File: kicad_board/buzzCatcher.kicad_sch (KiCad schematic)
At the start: 38 parts, among them IC1 TS02-66-60-BK-100-SCR-D, J1 95501-2661, J10 M5 Screw, J11 M5 Screw, J12 M5 Screw, J13 25 ft RJ12, J14 25 ft RJ12, J15 25 ft RJ12, J16 25 ft RJ12, J2 95501-2661, J3 95501-2661, J4 95501-2661, J5 95501-2661, J6 95501-2661, J7 95501-2661, J8 95501-2661, J9 M5 Screw, Q1 BS170, Q2 BS170, SW1 SW_Push, SW2 SW_Push, SW3 SW_Push, SW4 SW_Push

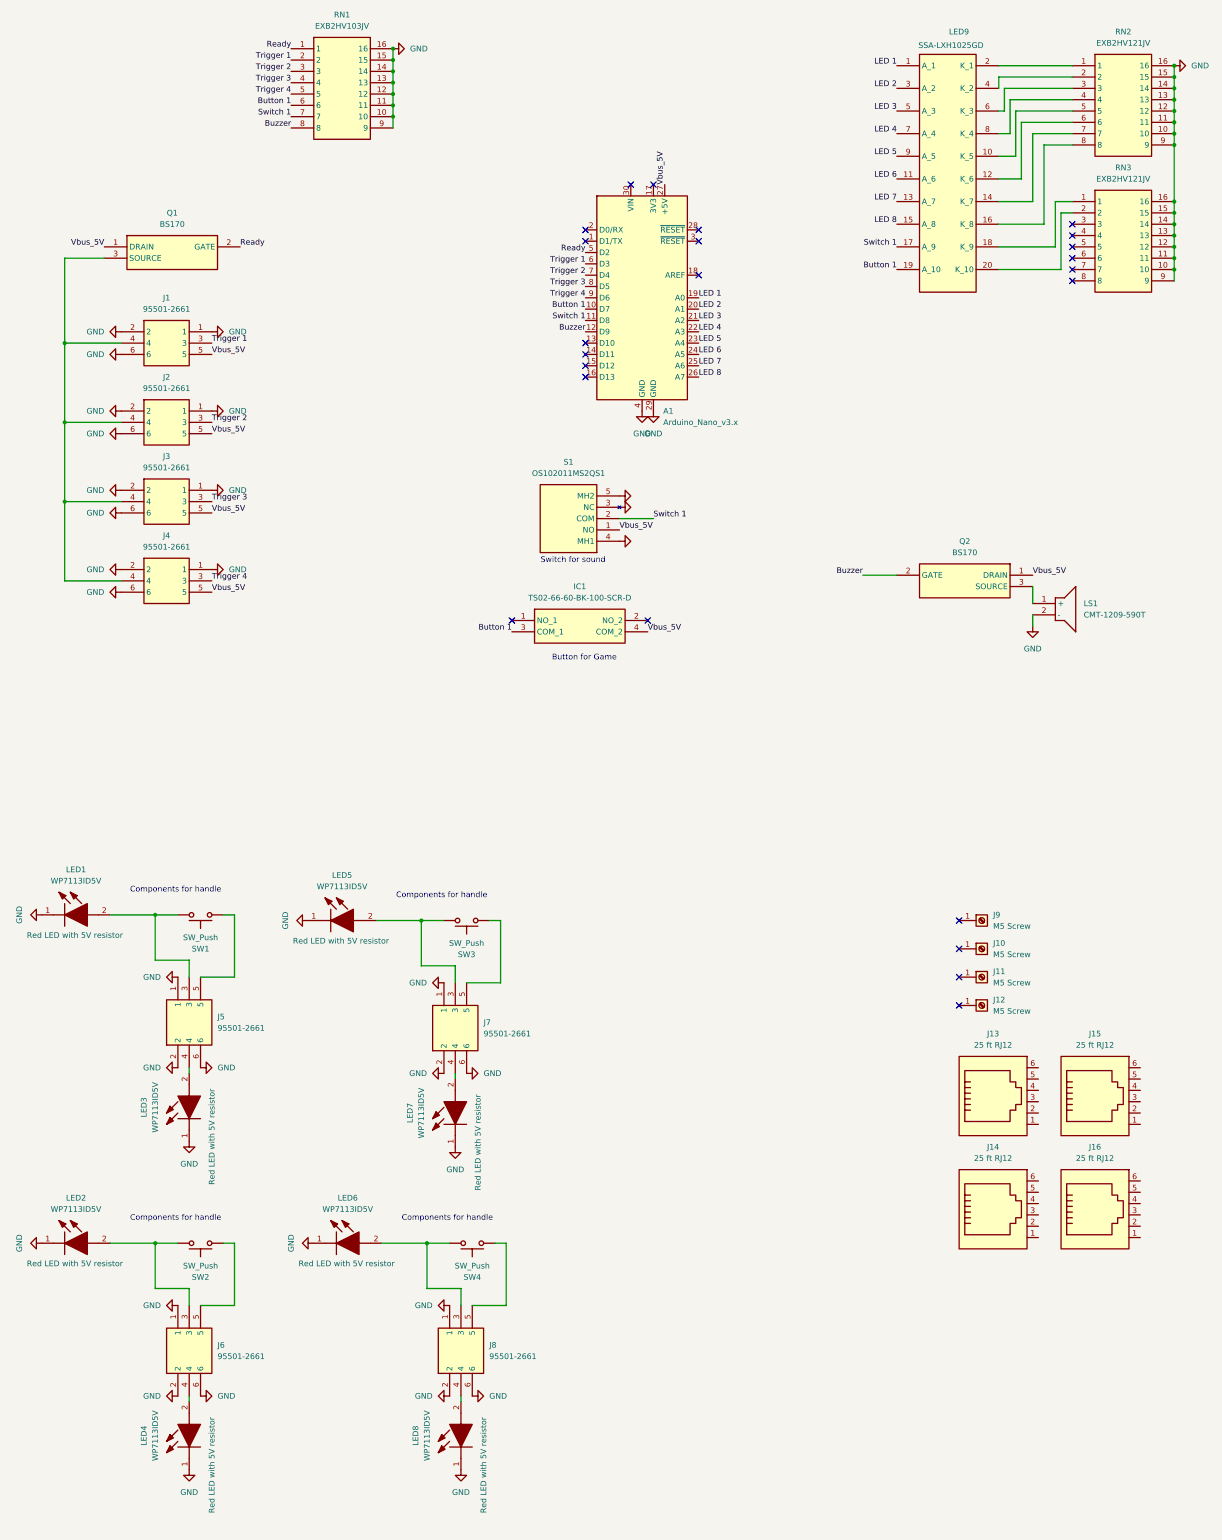
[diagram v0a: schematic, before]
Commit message: Added break out headers
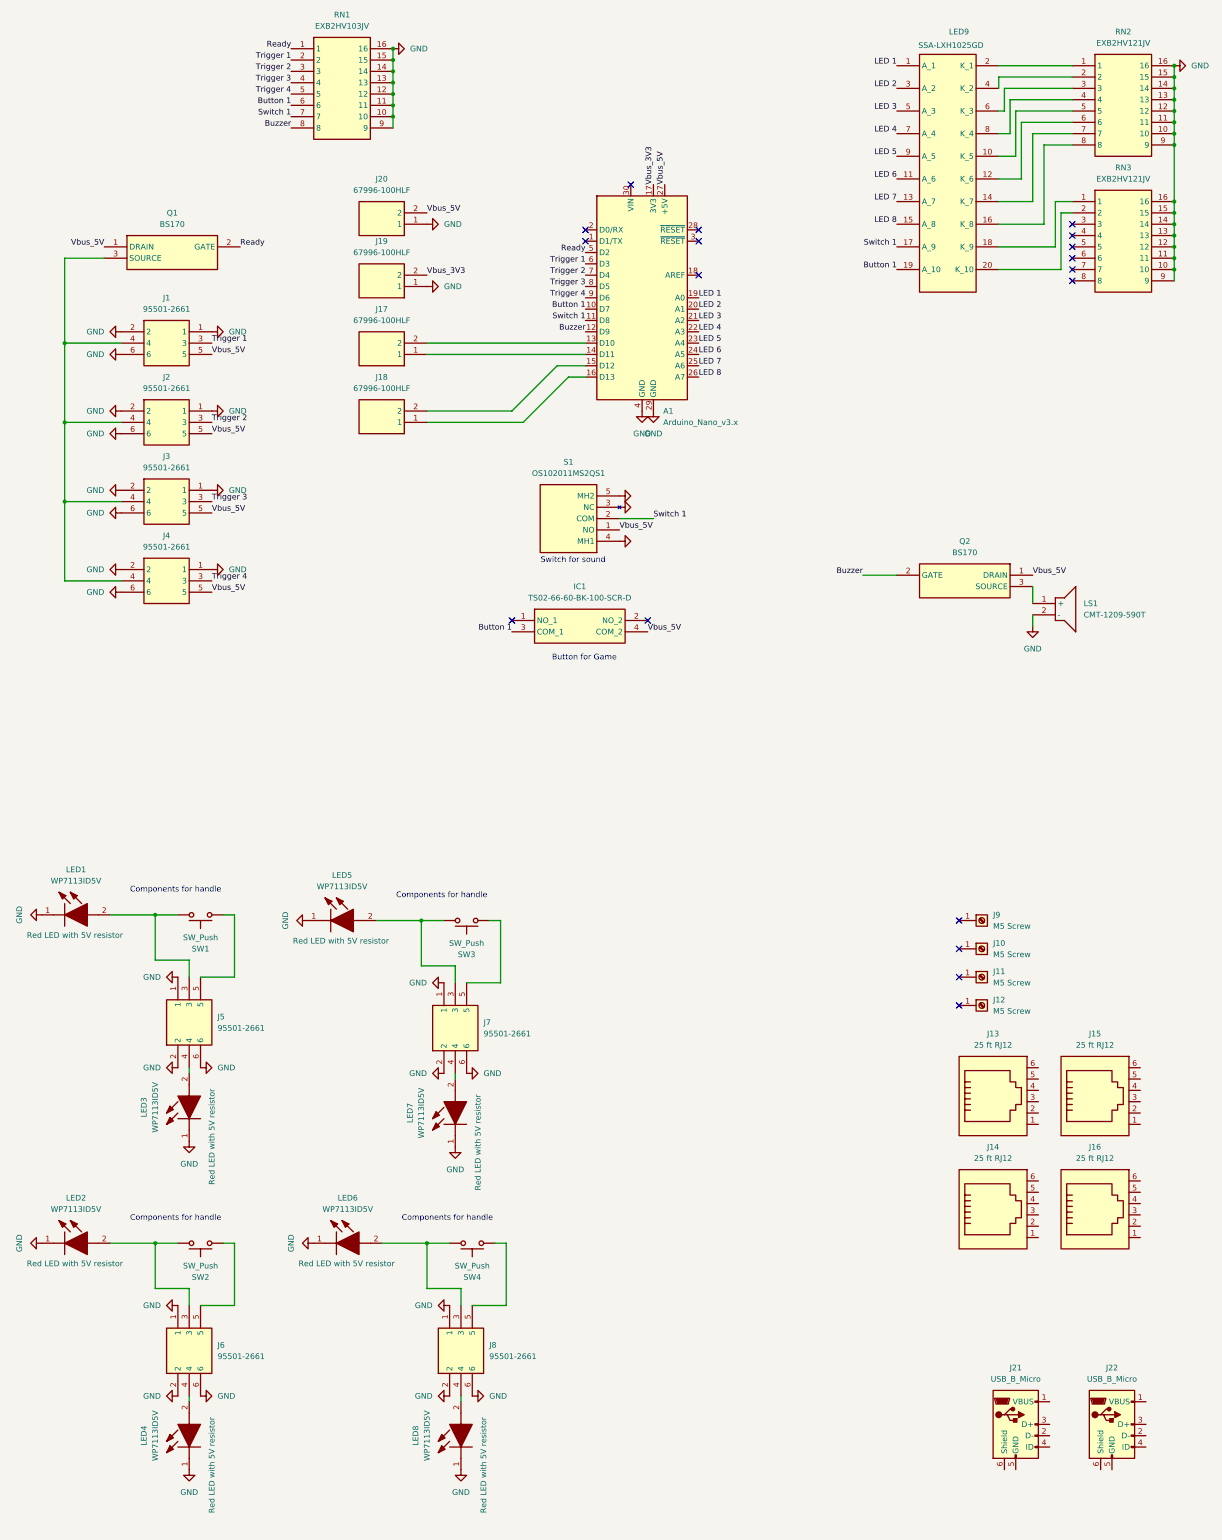
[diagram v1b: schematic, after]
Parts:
- added J17, J18, J19, J20: 67996-100HLF, HDRV2W67P254_2X1_254X483X858P, symbol SamacSys:67996-100HLF
- added J21, J22: USB_B_Micro, symbol Connector:USB_B_Micro
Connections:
- net GND: now also J19.1, J20.1
- net Vbus_5V: now also J20.2
- net at A1.13 (D10): now also J17.2
- net at A1.14 (D11): now also J17.1
- net at A1.15 (D12): now also J18.2
- net at A1.16 (D13): now also J18.1
- net Vbus_3V3: now reaches A1.17 (3V3)
- net Vbus_3V3: now also J19.2
- no-connect marks 23 -> 18

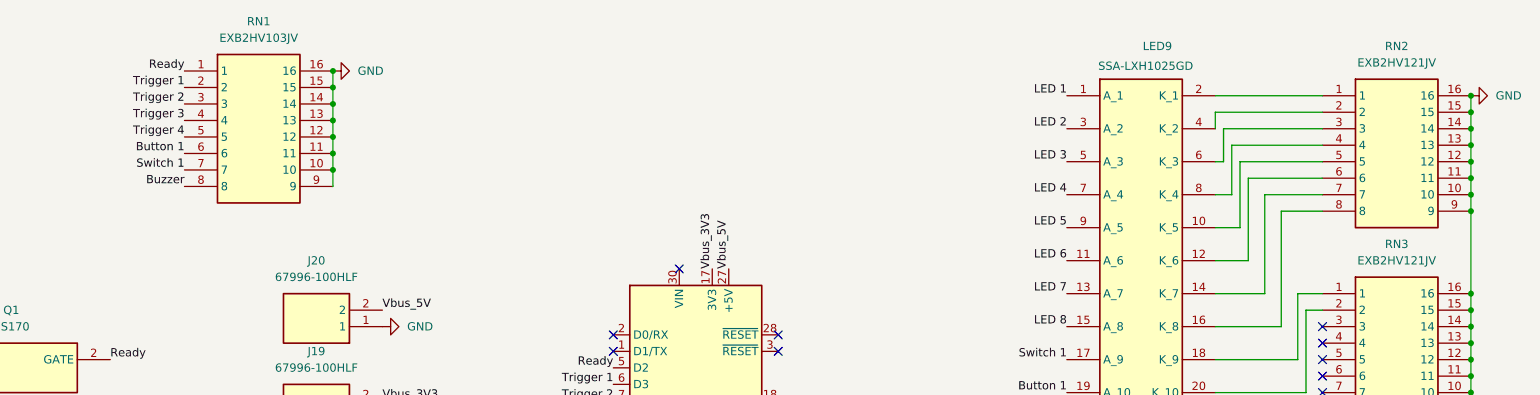
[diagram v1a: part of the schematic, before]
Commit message: Converted to bigger resistor pack
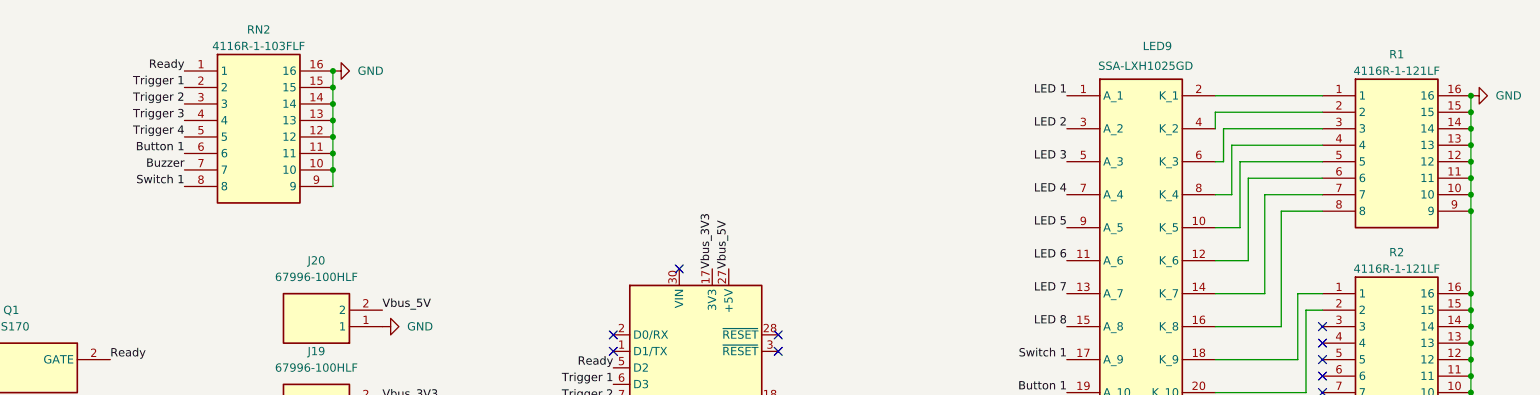
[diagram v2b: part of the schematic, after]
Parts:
- removed RN1: EXB2HV103JV, EXB2HV104JV, symbol SamacSys:EXB2HV103JV
- removed RN2, RN3: EXB2HV121JV, EXB2HV_1, symbol SamacSys:EXB2HV121JV
- added R1, R2: 4116R-1-121LF, DIP787W49P254L2197H469Q16N, symbol SamacSys:4116R-1-121LF
- added RN2: 4116R-1-103FLF, DIP787W49P254L2197H469Q16N, symbol SamacSys:4116R-1-103FLF
- J5, J6, J7, J8: footprint 95501-2661 -> (none)
- LED1, LED2, LED3, LED4, LED5, LED6, LED7, LED8: footprint WP7113ID5V -> (none)
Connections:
- net Button 1: now also RN2.6
- net Buzzer: now also RN2.7
- net GND: now also R1.10, R1.11, R1.12, R1.13, R1.14, R1.15, R1.16, R1.9, R2.10, R2.11, R2.12, R2.13, R2.14, R2.15, R2.16, R2.9, RN2.10, RN2.11, RN2.12, RN2.13, RN2.14, RN2.15, RN2.16, RN2.9
- net Ready: now also RN2.1
- net Switch 1: now also RN2.8
- net Trigger 1: now also RN2.2
- net Trigger 2: now also RN2.3
- net Trigger 3: now also RN2.4
- net Trigger 4: now also RN2.5
- net at LED9.18 (K_9): now also R2.1
- net at LED9.20 (K_10): now also R2.2
- net at LED9.10 (K_5): now also R1.5
- net at LED9.12 (K_6): now also R1.6
- net at LED9.14 (K_7): now also R1.7
- net at LED9.16 (K_8): now also R1.8
- net at LED9.2 (K_1): now also R1.1
- net at LED9.4 (K_2): now also R1.2
- net at LED9.6 (K_3): now also R1.3
- net at LED9.8 (K_4): now also R1.4

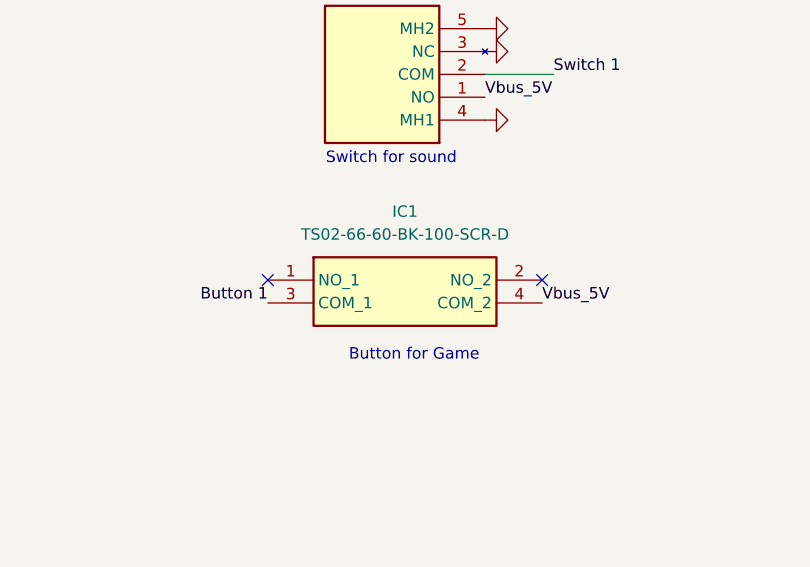
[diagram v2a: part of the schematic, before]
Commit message: Fixed Version 1.0 button pin error
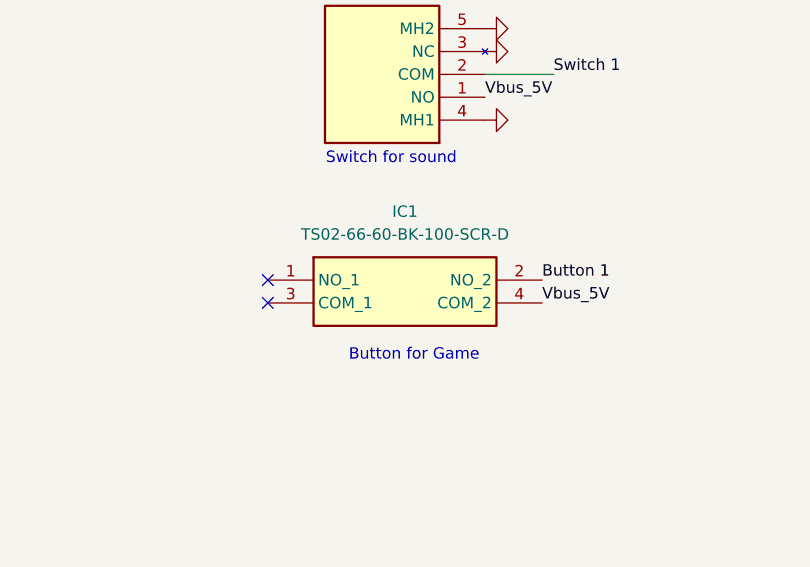
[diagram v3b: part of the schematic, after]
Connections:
- net Button 1: now also IC1.2 (NO_2); no longer IC1.3 (COM_1)
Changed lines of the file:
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@@
+	)
+	(no_connect
+		(at 124.46 153.67)
 	)
 	(no_connect
@@
 	)
 	(no_connect
-		(at 154.94 153.67)
-	)
-	(no_connect
-		(at 124.46 153.67)
+		(at 124.46 156.21)
 	)
 	(wire
@@
 	)
 	(label "Button 1"
-		(at 124.46 156.21 180)
-		(fields_autoplaced yes)
-		(effects
-			(font
-				(size 1.27 1.27)
-			)
-			(justify right bottom)
-		)
-	)
-	(label "Button 1"
 		(at 74.93 38.1 180)
 		(fields_autoplaced yes)
@@
 		(fields_autoplaced yes)
 		(effects
+			(font
+				(size 1.27 1.27)
+			)
+			(justify left bottom)
+		)
+	)
+	(label "Button 1"
+		(at 154.94 153.67 0)
+		(fields_autoplaced yes)
+		(effects

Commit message: Final tweaks after fabrication
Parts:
- J21: Manufacturer_Part_Number USB CABLE MICRO 80 -> UR050-010
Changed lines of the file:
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@@
 			)
 		)
-		(property "Manufacturer_Part_Number" "USB CABLE MICRO 80"
+		(property "Manufacturer_Part_Number" "UR050-010"
 			(at 237.49 334.01 0)
 			(effects

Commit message: Added manufacturing outputs
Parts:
- removed A1: Arduino_Nano_v3.x, Module:Arduino_Nano, symbol MCU_Module:Arduino_Nano_v3.x
- removed IC1: TS02-66-60-BK-100-SCR-D, TS026660BK100SCRD, symbol SamacSys:TS02-66-60-BK-100-SCR-D
- removed J1, J2, J3, J4: 95501-2661, 95501-2661, symbol SamacSys:95501-2661
- removed J10, J11, J12, J9: M5 Screw, symbol Connector:Screw_Terminal_01x01
- removed J13, J14, J15, J16: 25 ft RJ12, symbol Connector:RJ12
- removed J17, J18, J19, J20: 67996-100HLF, HDRV2W67P254_2X1_254X483X858P, symbol SamacSys:67996-100HLF
- removed J21, J22: USB_B_Micro, symbol Connector:USB_B_Micro
- removed J5, J6, J7, J8: 95501-2661, symbol SamacSys:95501-2661
- removed LED1, LED2, LED3, LED4, LED5, LED6, LED7, LED8: WP7113ID5V, symbol SamacSys:WP7113ID5V
- removed LED9: SSA-LXH1025GD, SSALXH1025GD, symbol SamacSys:SSA-LXH1025GD
- removed LS1: CMT-1209-590T, CMT1209590T, symbol SamacSys:CMT-1209-590T
- removed Q1, Q2: BS170, LM431ACZ, symbol SamacSys:BS170
- removed R1, R2: 4116R-1-121LF, DIP787W49P254L2197H469Q16N, symbol SamacSys:4116R-1-121LF
- removed RN2: 4116R-1-103FLF, DIP787W49P254L2197H469Q16N, symbol SamacSys:4116R-1-103FLF
- removed S1: OS102011MS2QS1, OS102011MS2QS1, symbol SamacSys:OS102011MS2QS1
- removed SW1, SW2, SW3, SW4: SW_Push, symbol Switch:SW_Push
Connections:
- no-connect marks 18 -> 0
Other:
- added sheet cables (cables.kicad_sch)
- added sheet handles (Handles.kicad_sch)
- added sheet motherboard (motherboard.kicad_sch)
- note removed: "Button for Game"
- note removed: "Components for handle"
- note removed: "Switch for sound"
